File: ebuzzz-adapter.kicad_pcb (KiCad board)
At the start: 2 copper layers, 80 x 20 mm, 35 parts, among them J1 Conn_01x04, J2 Conn_01x04, J3 Conn_01x06, J4 EBUS, Q1 BC817-40, U1 CNY17-4, U2 CNY17-4, U3 LM2903, U4 LP2951-5.0_SOIC

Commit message: Version 1 release (hardware tested)
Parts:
- added D6: 1N4148WS, Diode_SMD:D_SOD-323, F.Cu at (157.0, 74.4)
- R16: value 10E -> 120E
- moved J3 12.8 mm to (109.5, 85.4), turned to 180 degrees
- moved R10 5.18 mm to (142.2, 84.0), turned to 90 degrees
- moved R1 5.00 mm to (113.8, 80.6), turned to 180 degrees
- moved C3 3.61 mm to (132.7, 84.9)
- moved R9 3.47 mm to (144.4, 84.0)
- moved R16 1.76 mm to (156.8, 71.5), turned to 0 degrees
- moved R4 1.63 mm to (113.8, 78.4), turned to 0 degrees
- moved D1 1.42 mm to (113.8, 76.2), turned to 0 degrees
- moved R11 0.68 mm to (143.4, 87.0), turned to 180 degrees
- moved R2 0.28 mm to (113.8, 82.8), turned to 0 degrees
- moved R5 0.17 mm to (129.8, 86.2)
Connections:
- R10 pad 1: +5V -> Net-(R10-Pad1)
- R11 pad 1: Net-(R10-Pad2) -> +5V
- R11 pad 2: +5V -> Net-(R10-Pad1)
- R12 pad 1: +5V -> Net-(R10-Pad1)
- R16 pad 2: /ebus-signal -> Net-(D6-Pad1)
- R9 pad 1: Net-(R10-Pad2) -> +5V
- R9 pad 2: Net-(R9-Pad2) -> Net-(R10-Pad2)
- U3 pad 1: Net-(R9-Pad2) -> Net-(R10-Pad2)
- U3 pad 3: +5V -> Net-(R10-Pad1)
- U3 pad 5: +5V -> Net-(R10-Pad1)
- U3 pad 6: Net-(R9-Pad2) -> Net-(R10-Pad2)
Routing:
- net Net-(R10-Pad1): track 0.00 -> 27.1 mm, vias 0 -> 2
- net Net-(R9-Pad2): track 8.90 -> 0.00 mm
- net Net-(R10-Pad2): track 7.30 -> 12.1 mm
- net GND: track 21.8 -> 25.6 mm
- net /uart_3v3: track 0.00 -> 3.05 mm
- net /uart_rx: track 20.8 -> 18.3 mm
- net Net-(D6-Pad1): track 0.00 -> 2.46 mm
- net Net-(C1-Pad1): track 13.0 -> 10.6 mm
- net /ebus-signal: track 24.6 -> 22.2 mm
- net +5V: track 4.49 -> 6.61 mm
- net /uart_tx: track 11.1 -> 9.90 mm
- net Net-(Q1-Pad1): track 34.6 -> 34.0 mm
- net Net-(R1-Pad2): track 2.72 -> 2.21 mm
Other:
- board text added: "v1"

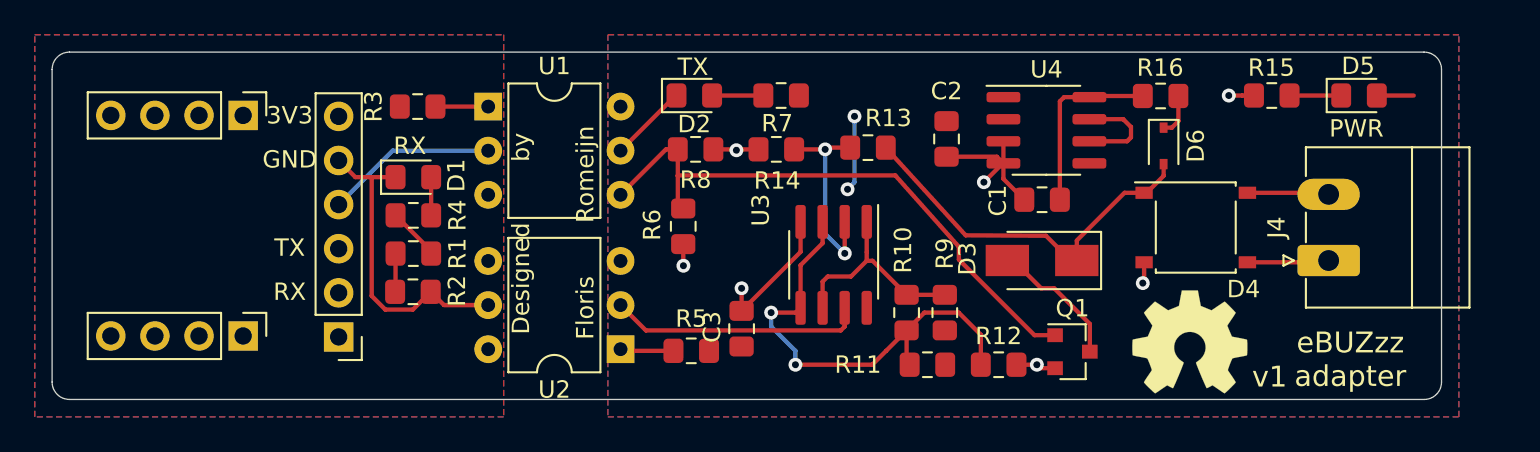
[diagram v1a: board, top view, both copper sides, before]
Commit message: added LCSC components (and tuned values)
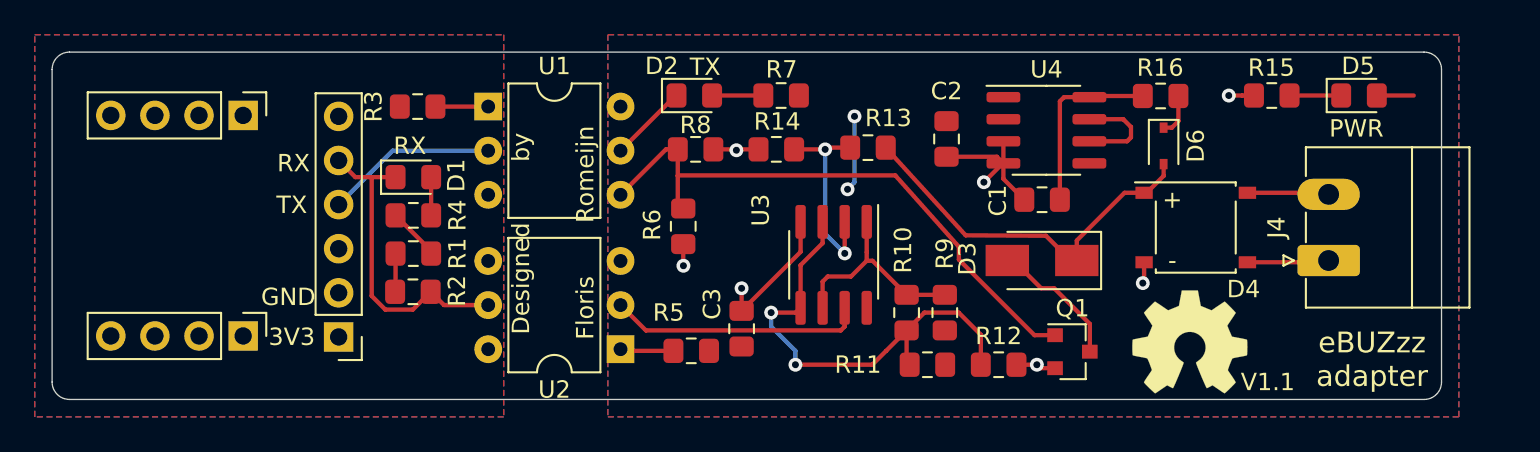
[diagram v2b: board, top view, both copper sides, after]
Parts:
- D1: value tx green -> DNF RX green
- D2: value rx red -> TX red
- D3: value Z1SMAxxx -> 1SMB5924BY3G
- R1, R2, R4: value 470 -> DNF 470
- U3: value LM2903 -> LM2903DT
- U4: value LP2951-5.0_SOIC -> LP2951-50DR
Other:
- board text added: "+"
- board text added: "-"
- board text added: "V1.1"
- board text removed: "v1"

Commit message: replace external board with onboard CP2104
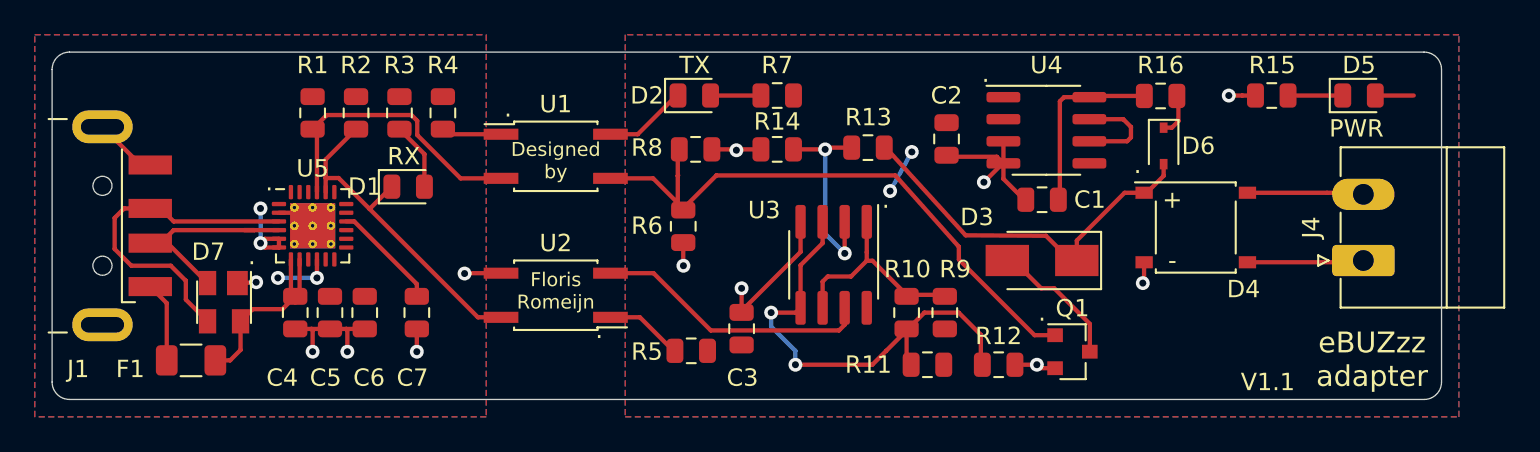
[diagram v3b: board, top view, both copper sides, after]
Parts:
- removed J2: Conn_01x04, Connector_PinHeader_2.54mm:PinHeader_1x04_P2.54mm_Vertical
- removed J3: Conn_01x06, Connector_PinHeader_2.54mm:PinHeader_1x06_P2.54mm_Vertical
- removed REF** (x2): OSHW-Symbol_6.7x6mm_SilkScreen, Symbol:OSHW-Symbol_6.7x6mm_SilkScreen
- added C4: 1u, Capacitor_SMD:C_0805_2012Metric, F.Cu at (107.0, 84.0)
- added C5: 100n, Capacitor_SMD:C_0805_2012Metric, F.Cu at (109.0, 84.0)
- added C6: 4.7u, Capacitor_SMD:C_0805_2012Metric, F.Cu at (111.0, 84.0)
- added C7: DNF, Capacitor_SMD:C_0805_2012Metric, F.Cu at (114.0, 84.0)
- added D7: SP0503BAHT, Package_TO_SOT_SMD:SOT-143, F.Cu at (102.9, 83.4)
- added F1: 1A, Fuse:Fuse_1206_3216Metric, F.Cu at (101.0, 86.8)
- added U5: CP2104, Package_DFN_QFN:QFN-24-1EP_4x4mm_P0.5mm_EP2.6x2.6mm_ThermalVias, F.Cu at (108.0, 79.0)
- C1, C2, C3: footprint Capacitor_SMD:C_0805_2012Metric_Pad1.15x1.40mm_HandSolder -> Capacitor_SMD:C_0805_2012Metric
- D1: value DNF RX green -> RX green; footprint LED_SMD:LED_0805_2012Metric_Pad1.15x1.40mm_HandSolder -> LED_SMD:LED_0805_2012Metric
- D2, D5: footprint LED_SMD:LED_0805_2012Metric_Pad1.15x1.40mm_HandSolder -> LED_SMD:LED_0805_2012Metric
- J1: value Conn_01x04 -> USB_A; footprint Connector_PinHeader_2.54mm:PinHeader_1x04_P2.54mm_Vertical -> Connector_USB:USB_A_CNCTech_1001-011-01101_Horizontal
- R1, R2: value DNF 470 -> DNF; footprint Resistor_SMD:R_0805_2012Metric_Pad1.15x1.40mm_HandSolder -> Resistor_SMD:R_0805_2012Metric
- R10, R11, R12, R13, R14, R15, R16, R6, R7, R8, R9: footprint Resistor_SMD:R_0805_2012Metric_Pad1.15x1.40mm_HandSolder -> Resistor_SMD:R_0805_2012Metric
- R3: value 470 -> 1k; footprint Resistor_SMD:R_0805_2012Metric_Pad1.15x1.40mm_HandSolder -> Resistor_SMD:R_0805_2012Metric
- R4: value DNF 470 -> 470; footprint Resistor_SMD:R_0805_2012Metric_Pad1.15x1.40mm_HandSolder -> Resistor_SMD:R_0805_2012Metric
- R5: value 470 -> 2.2k; footprint Resistor_SMD:R_0805_2012Metric_Pad1.15x1.40mm_HandSolder -> Resistor_SMD:R_0805_2012Metric
- U1, U2: value CNY17-4 -> LTV-357T; footprint Package_DIP:DIP-6_W7.62mm -> Package_SO:SO-4_4.4x3.6mm_P2.54mm
- moved J1 16.3 mm to (89.0, 79.0), turned to 180 degrees
- moved R2 10.8 mm to (110.5, 72.5), turned to 270 degrees
- moved R1 9.96 mm to (108.0, 72.5), turned to 270 degrees
- moved R4 6.14 mm to (115.5, 72.5), turned to 270 degrees
- moved U2 4.85 mm to (122.0, 83.0)
- moved U1 4.83 mm to (122.0, 75.0)
- moved J4 2.00 mm to (168.5, 81.0)
- moved R3 1.11 mm to (113.0, 72.5), turned to 270 degrees
- moved D1 0.63 mm to (113.5, 76.8)
- moved R7 0.22 mm to (134.8, 71.5)
- moved R14 0.05 mm to (134.8, 74.6)
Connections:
- D1 pad 1: /uart_rx -> /RX
- J1 pad 2: Net-(J1-Pad2) -> /D-
- J1 pad 3: Net-(J1-Pad3) -> /D+
- J1 pad 4: Net-(J1-Pad4) -> GNDREF
- R1 pad 1: /uart_3v3 -> VCC
- R1 pad 2: Net-(R1-Pad2) -> /TX
- R2 pad 1: Net-(R1-Pad2) -> VCC
- R2 pad 2: /uart_rx -> /RX
- R3 pad 1: /uart_3v3 -> VCC
- R3 pad 2: Net-(R3-Pad2) -> Net-(D1-Pad2)
- R4 pad 1: /uart_3v3 -> VCC
- R4 pad 2: Net-(D1-Pad2) -> Net-(R4-Pad2)
- U1 pad 1: Net-(R3-Pad2) -> Net-(R4-Pad2)
- U1 pad 2: /uart_tx -> /TX
- U1 pad 3: Net-(U1-Pad3) -> Net-(Q1-Pad1)
- U1 pad 4: Net-(Q1-Pad1) -> Net-(D2-Pad1)
- U2 pad 3: Net-(U2-Pad3) -> GNDREF
- U2 pad 4: /uart_gnd -> /RX
- U4 pad 5: Net-(U4-Pad5) -> (no net)
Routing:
- net /RX: track 0.00 -> 19.6 mm
- net /D+: track 0.00 -> 19.0 mm
- net /uart_rx: track 18.3 -> 0.00 mm
- net GNDREF: track 0.00 -> 17.1 mm, vias 0 -> 5
- net /TX: track 0.00 -> 16.9 mm
- net /D-: track 0.00 -> 12.0 mm
- net VBUS: track 0.00 -> 11.9 mm
- net /uart_tx: track 9.90 -> 0.00 mm
- net VCC: track 0.00 -> 8.14 mm, vias 0 -> 4
- net Net-(C7-Pad1): track 0.00 -> 6.27 mm
- net Net-(F1-Pad1): track 0.00 -> 4.64 mm
- net Net-(R4-Pad2): track 0.00 -> 3.47 mm
- net Net-(R3-Pad2): track 3.17 -> 0.00 mm
- net /uart_3v3: track 3.05 -> 0.00 mm
- net Net-(R1-Pad2): track 2.21 -> 0.00 mm
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- added copper zone on B.Cu, net GNDREF
- added copper zone on F.Cu, net VCC
- removed copper zone on F.Cu, net /uart_3v3
- removed copper zone on B.Cu, net /uart_gnd
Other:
- board text added: "."
- board text removed: "3V3"
- board text removed: "GND"

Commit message: added manufacturing files
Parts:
- J1: footprint Connector_USB:USB_A_CNCTech_1001-011-01101_Horizontal -> ebuzzz-adapter:XKB_Connectivity_U217-041N-4BV81
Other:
- board text added: "V1.2"
- board text removed: "V1.1"

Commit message: Updated PCB.
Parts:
- D7: value SP0503BAHT -> TPSP0503BAHTG
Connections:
- U4 pad 5: (no net) -> unconnected-(U4-Pad5)
- U5 pad 1: (no net) -> unconnected-(U5-Pad1)
- U5 pad 10: VCC -> unconnected-(U5-Pad10)
- U5 pad 11: (no net) -> unconnected-(U5-Pad11)
- U5 pad 12: (no net) -> unconnected-(U5-Pad12)
- U5 pad 13: (no net) -> unconnected-(U5-Pad13)
- U5 pad 14: (no net) -> unconnected-(U5-Pad14)
- U5 pad 15: (no net) -> unconnected-(U5-Pad15)
- U5 pad 17: (no net) -> unconnected-(U5-Pad17)
- U5 pad 18: (no net) -> unconnected-(U5-Pad18)
- U5 pad 19: (no net) -> unconnected-(U5-Pad19)
- U5 pad 2: GNDREF -> Net-(U5-Pad2)
- U5 pad 22: (no net) -> unconnected-(U5-Pad22)
- U5 pad 23: (no net) -> unconnected-(U5-Pad23)
- U5 pad 24: (no net) -> unconnected-(U5-Pad24)
- U5 pad 25: GNDREF -> Net-(U5-Pad2)
- U5 pad 5: VCC -> unconnected-(U5-Pad5)
- U5 pad 7: VBUS -> VCC
- U5 pad 9: (no net) -> VBUS
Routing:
- net VCC: track 8.14 -> 0.00 mm, vias 4 -> 0
- net unconnected-(U5-Pad5): track 0.00 -> 4.83 mm, vias 0 -> 2
- net unconnected-(U5-Pad10): track 0.00 -> 3.31 mm, vias 0 -> 2
- net Net-(U5-Pad2): track 0.00 -> 2.25 mm
- net GNDREF: track 17.1 -> 14.8 mm
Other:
- net class Default removed
